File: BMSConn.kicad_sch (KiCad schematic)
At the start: 0 parts

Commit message: mostly done afe ic
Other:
- note added: "pulse transformer, battery monitor connections, isouart goes on stm side"
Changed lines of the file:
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@@
 	(generator_version "10.0")
 	(paper "A4")
+	(text "pulse transformer, battery monitor connections, isouart goes on stm side"
+		(exclude_from_sim no)
+		(at 157.734 121.412 0)
+		(effects
+			(font
+				(size 1.27 1.27)
+			)
+		)
+	)
 )

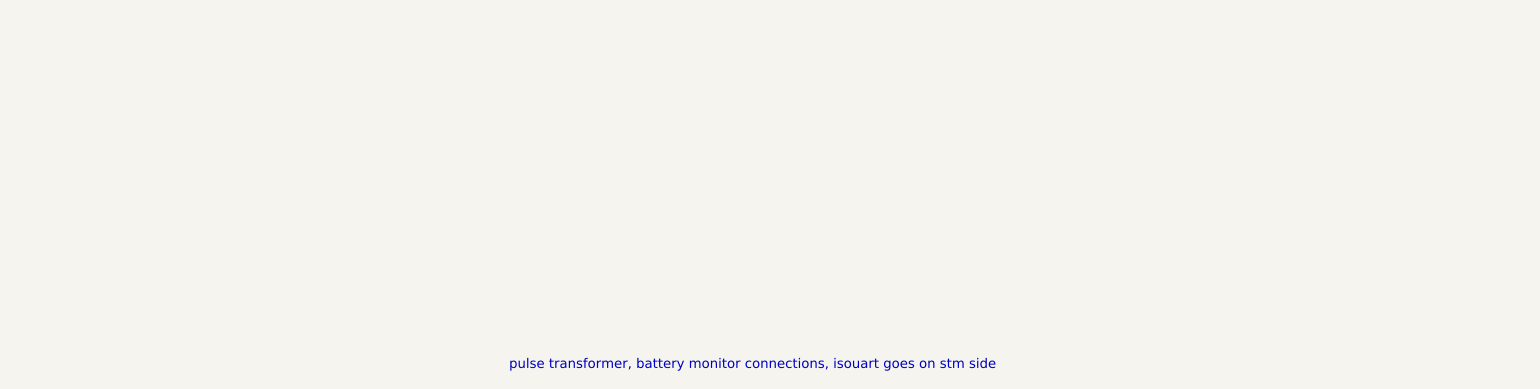
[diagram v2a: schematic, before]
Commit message: schematic done except for pulse transformer
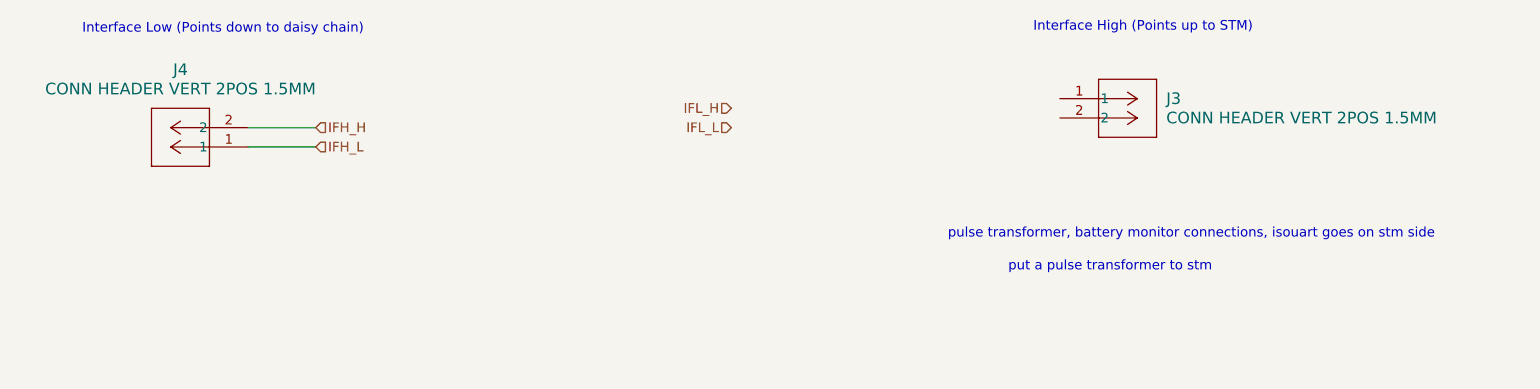
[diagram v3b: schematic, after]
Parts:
- added J3, J4: CONN HEADER VERT 2POS 1.5MM, footprints:CONN_B2B-ZR_02P_JST, symbol symbols:B2B-ZR
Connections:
- new net IFH_H: J4.2
- new net IFH_L: J4.1
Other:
- note added: "Interface High (Points up to STM)"
- note added: "Interface Low (Points down to daisy chain)"
- note added: "put a pulse transformer to stm"

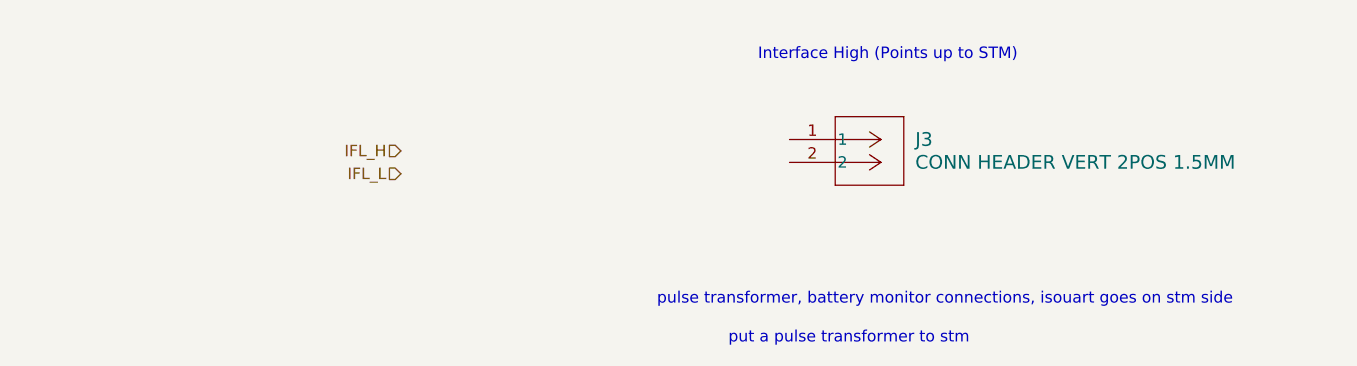
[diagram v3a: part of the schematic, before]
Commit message: fixed balancing module and added pulse transformer
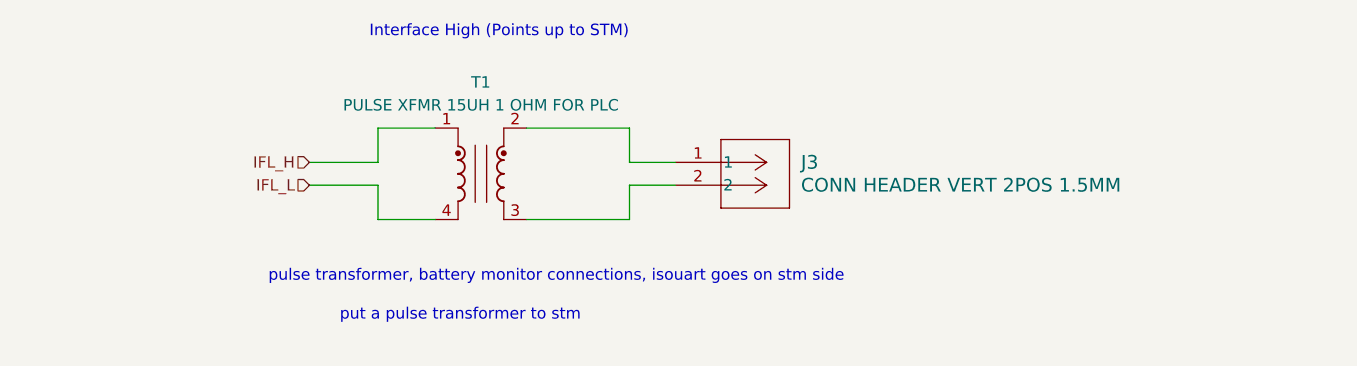
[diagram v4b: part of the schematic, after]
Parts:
- added T1: PULSE XFMR 15UH 1 OHM FOR PLC, footprints:AMT45S-150-2P-TL000, symbol symbols:AMT45S-150-2P-TL000
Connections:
- net IFL_H: now also T1.1
- net IFL_L: now also T1.4
- net at J3.1: now also T1.2
- net at J3.2: now also T1.3
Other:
- moved on the sheet: J3
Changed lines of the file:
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@@
 	(text "Interface High (Points up to STM)"
 		(exclude_from_sim no)
-		(at 209.042 76.962 0)
+		(at 165.862 74.422 0)
 		(effects
 			(font
@@
 	(text "put a pulse transformer to stm"
 		(exclude_from_sim no)
-		(at 204.724 108.458 0)
+		(at 161.544 105.918 0)
 		(effects
 			(font
@@
 	(text "pulse transformer, battery monitor connections, isouart goes on stm side"
 		(exclude_from_sim no)
-		(at 215.392 104.14 0)
+		(at 172.212 101.6 0)
 		(effects
 			(font
@@
 	(wire
 		(pts
+			(xy 168.91 85.09) (xy 180.34 85.09)
+		)
+		(stroke
+			(width 0)
+			(type default)
+		)
+	)
+	(wire
+		(pts
+			(xy 144.78 91.44) (xy 152.4 91.44)
+		)
+		(stroke
+			(width 0)
+			(type default)
+		)
+	)
+	(wire
+		(pts
+			(xy 180.34 91.44) (xy 185.42 91.44)
+		)
+		(stroke
+			(width 0)
+			(type default)
+		)
+	)
+	(wire
+		(pts
+			(xy 180.34 85.09) (xy 180.34 88.9)
+		)
+		(stroke
+			(width 0)
+			(type default)
+		)
+	)
+	(wire
+		(pts
+			(xy 168.91 95.25) (xy 180.34 95.25)
+		)
+		(stroke
+			(width 0)
+			(type default)
+		)
+	)
+	(wire
+		(pts
+			(xy 152.4 95.25) (xy 158.75 95.25)
+		)
+		(stroke
+			(width 0)
+			(type default)
+		)
+	)
+	(wire
+		(pts
+			(xy 152.4 88.9) (xy 152.4 85.09)
+		)
+		(stroke
+			(width 0)
+			(type default)
+		)
+	)
+	(wire
+		(pts
+			(xy 180.34 88.9) (xy 185.42 88.9)
+		)
+		(stroke
+			(width 0)
+			(type default)
+		)
+	)
+	(wire
+		(pts
+			(xy 152.4 91.44) (xy 152.4 95.25)
+		)
+		(stroke
+			(width 0)
+			(type default)
+		)
+	)
+	(wire
+		(pts
 			(xy 91.44 92.71) (xy 100.33 92.71)
+		)
+		(stroke
+			(width 0)
+			(type default)
+		)
+	)
+	(wire
+		(pts
+			(xy 144.78 88.9) (xy 152.4 88.9)
+		)
+		(stroke
+			(width 0)
+			(type default)
+		)
+	)
+	(wire
+		(pts
+			(xy 152.4 85.09) (xy 158.75 85.09)
+		)
+		(stroke
+			(width 0)
+			(type default)
+		)
+	)
+	(wire
+		(pts
+			(xy 180.34 95.25) (xy 180.34 91.44)
 		)
 		(stroke
@@
 	(hierarchical_label "IFL_L"
 		(shape input)
-		(at 154.94 90.17 180)
+		(at 144.78 91.44 180)
 		(effects
 			(font
@@
 	(hierarchical_label "IFL_H"
 		(shape input)
-		(at 154.94 87.63 180)
+		(at 144.78 88.9 180)
 		(effects
 			(font
@@
 	(symbol
 		(lib_id "symbols:B2B-ZR")
-		(at 198.12 86.36 0)
+		(at 185.42 88.9 0)
 		(unit 1)
 		(body_style 1)
@@
 		(fields_autoplaced yes)
 		(property "Reference" "J3"
-			(at 212.09 86.3599 0)
+			(at 199.39 88.8999 0)
 			(show_name no)
 			(do_not_autoplace no)
@@
 		)
 		(property "Value" "CONN HEADER VERT 2POS 1.5MM"
-			(at 212.09 88.8999 0)
+			(at 199.39 91.4399 0)
 			(show_name no)
 			(do_not_autoplace no)
@@
 		)
 		(property "Footprint" "footprints:CONN_B2B-ZR_02P_JST"
-			(at 198.12 86.36 0)
+			(at 185.42 88.9 0)
 			(hide yes)
 			(show_name no)
@@
 		)
 		(property "Datasheet" "https://www.digikey.ca/en/products/detail/jst-sales-america-inc/B2B-ZR/926564"
-			(at 198.12 86.36 0)
+			(at 185.42 88.9 0)
 			(hide yes)
 			(show_name no)
@@
 		)
 		(property "Description" "Connector Header Through Hole 2 position 0.059\" (1.50mm)"
-			(at 198.12 86.36 0)
+			(at 185.42 88.9 0)
 			(hide yes)
 			(show_name no)
@@
 					(unit 1)
 				)
+			)
+		)
+	)
+	(symbol
+		(lib_id "symbols:AMT45S-150-2P-TL000")
+		(at 163.83 90.17 0)
+		(unit 1)
+		(body_style 1)
+		(exclude_from_sim no)
+		(in_bom yes)
+		(on_board yes)
+		(in_pos_files yes)
+		(dnp no)
+		(fields_autoplaced yes)
+		(property "Reference" "T1"
+			(at 163.83 80.01 0)
+			(show_name no)
+			(do_not_autoplace no)
+			(effects
+				(font
+					(size 1.27 1.27)
+				)
+			)
+		)
+		(property "Value" "PULSE XFMR 15UH 1 OHM FOR PLC"
+			(at 163.83 82.55 0)
+			(show_name no)
+			(do_not_autoplace no)
+			(effects
+				(font
+					(size 1.27 1.27)
+				)
+			)
+		)
+		(property "Footprint" "footprints:AMT45S-150-2P-TL000"
+			(at 163.83 90.17 0)
+			(hide yes)
+			(show_name no)
+			(do_not_autoplace no)
+			(effects
+				(font
+					(size 1.27 1.27)
+				)
+			)
+		)
+		(property "Datasheet" "https://www.digikey.ca/en/products/detail/tdk/AMT45S-150-2P-TL000/28724340"
+			(at 156.21 90.17 0)
+			(hide yes)
+			(show_name no)
+			(do_not_autoplace no)
+			(effects
+				(font
+					(size 1.27 1.27)
+				)
+			)
+		)
+		(property "Description" "15µH General Purpose Pulse Transformer Surface Mount"
+			(at 163.83 90.17 0)
+			(hide yes)
+			(show_name no)
+			(do_not_autoplace no)
+			(effects
+				(font
+					(size 1.27 1.27)
+				)
+			)
+		)
+		(pin "1"
+		)
+		(pin "4"
+		)
+		(pin "2"
+		)
+		(pin "3"
+		)
+		(instances
+			(project "bms-afe"
+				(path "/226a23e7-09bb-40bc-b53a-ec42a6b7cc90/6d53ec20-967d-414a-950d-119f66d4f6c2"
+					(reference "T1")
+					(unit 1)
+				)

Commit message: finished schematic
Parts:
- added R4, R5: 0, symbol Device:R_Small_US
- renumbered J4 to J2
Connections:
- net IFL_H: now also R4.1
- net IFL_L: now also R5.1
- net at J3.1, T1.2: now also R4.2
- net at J3.2, T1.3: now also R5.2
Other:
- moved on the sheet: T1

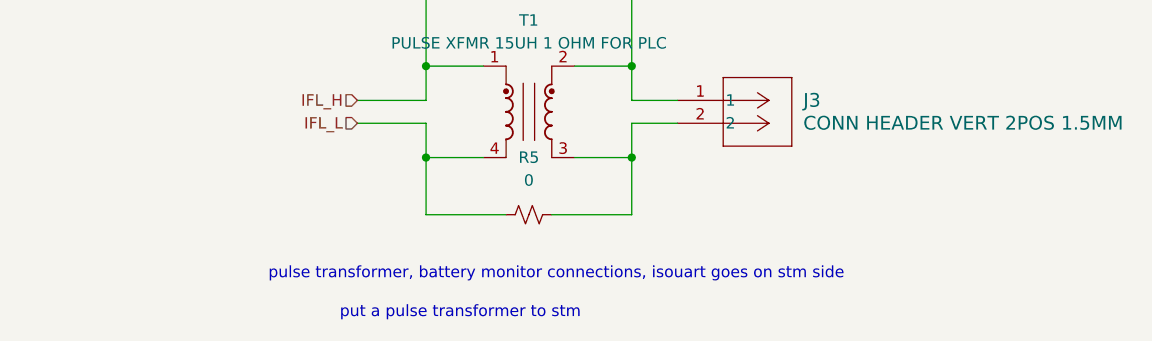
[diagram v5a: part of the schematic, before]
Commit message: added led resistor
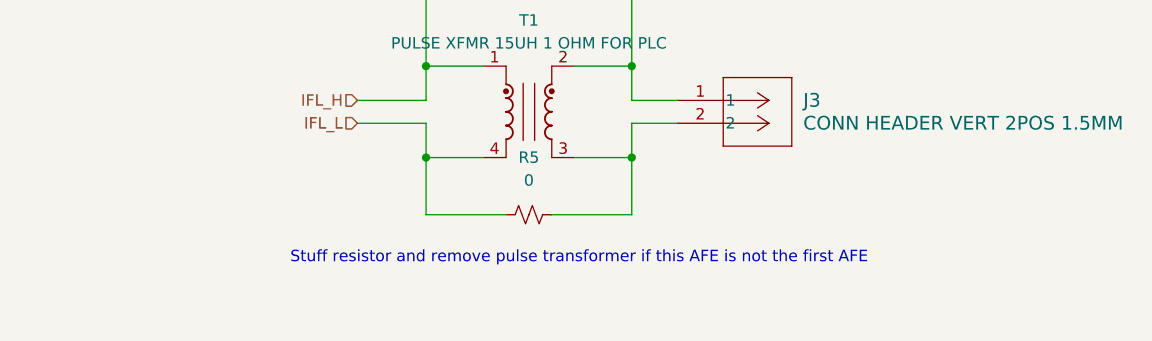
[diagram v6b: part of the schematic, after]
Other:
- note added: "Stuff resistor and remove pulse transformer if this AFE is not the first AFE"
- note removed: "pulse transformer, battery monitor connections, isouart goes on stm side"
- note removed: "put a pulse transformer to stm"
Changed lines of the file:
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@@
 		)
 	)
-	(text "put a pulse transformer to stm"
+	(text "Stuff resistor and remove pulse transformer if this AFE is not the first AFE"
 		(exclude_from_sim no)
-		(at 161.29 112.522 0)
+		(at 174.498 106.426 0)
 		(effects
 			(font
-				(size 1.27 1.27)
-			)
-		)
-	)
-	(text "pulse transformer, battery monitor connections, isouart goes on stm side"
-		(exclude_from_sim no)
-		(at 171.958 108.204 0)
-		(effects
-			(font

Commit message: fixed minor changes
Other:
- note added: "Interface High (Points up to STM OR next AFE if used in daisy chain)"
- note removed: "Interface High (Points up to STM)"
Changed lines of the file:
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@@
 	(generator_version "10.0")
 	(paper "A4")
-	(text "Interface High (Points up to STM)"
+	(text "Interface High (Points up to STM OR next AFE if used in daisy chain)"
 		(exclude_from_sim no)
-		(at 164.592 63.5 0)
+		(at 171.196 65.278 0)
 		(effects
 			(font

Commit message: passive values
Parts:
- added C50: CAP CER 0.33UF 16V X7R 0603, Capacitor_SMD:C_0603_1608Metric, symbol Device:C_Small
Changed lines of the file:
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@@
+	)
+	(symbol
+		(lib_id "Device:C_Small")
+		(at 1.6891 2.9211 0)
+		(unit 1)
+		(body_style 1)
+		(exclude_from_sim no)
+		(in_bom yes)
+		(on_board yes)
+		(in_pos_files yes)
+		(dnp no)
+		(fields_autoplaced yes)
+		(property "Reference" "C50"
+			(at 4.2291 1.6573 0)
+			(show_name no)
+			(do_not_autoplace no)
+			(effects
+				(font
+					(size 1.27 1.27)
+				)
+				(justify left)
+			)
+		)
+		(property "Value" "CAP CER 0.33UF 16V X7R 0603"
+			(at 4.2291 4.1973 0)
+			(show_name no)
+			(do_not_autoplace no)
+			(effects
+				(font
+					(size 1.27 1.27)
+				)
+				(justify left)
+			)
+		)
+		(property "Footprint" "Capacitor_SMD:C_0603_1608Metric"
+			(at 1.6891 2.9211 0)
+			(hide yes)
+			(show_name no)
+			(do_not_autoplace no)
+			(effects
+				(font
+					(size 1.27 1.27)
+				)
+			)
+		)
+		(property "Datasheet" "https://www.digikey.ca/en/products/detail/samsung-electro-mechanics/CL10B334KO8NNNC/3887706"
+			(at 1.6891 2.9211 0)
+			(hide yes)
+			(show_name no)
+			(do_not_autoplace no)
+			(effects
+				(font
+					(size 1.27 1.27)
+				)
+			)
+		)
+		(property "Description" "0.33 µF ±10% 16V Ceramic Capacitor X7R 0603 (1608 Metric)"
+			(at 1.6891 2.9211 0)
+			(hide yes)
+			(show_name no)
+			(do_not_autoplace no)
+			(effects
+				(font
+					(size 1.27 1.27)
+				)
+			)
+		)
+		(pin "2"
+		)
+		(pin "1"
+		)
+		(instances
+			(project "bms-afe"
+				(path "/226a23e7-09bb-40bc-b53a-ec42a6b7cc90/6d53ec20-967d-414a-950d-119f66d4f6c2"
+					(reference "C50")
+					(unit 1)
+				)
+			)
+		)
 	)
 	(symbol
